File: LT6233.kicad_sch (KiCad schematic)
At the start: 15 parts, among them U3001 LT6233CS6#TRMPBF, U3002 PBSS4230T,215

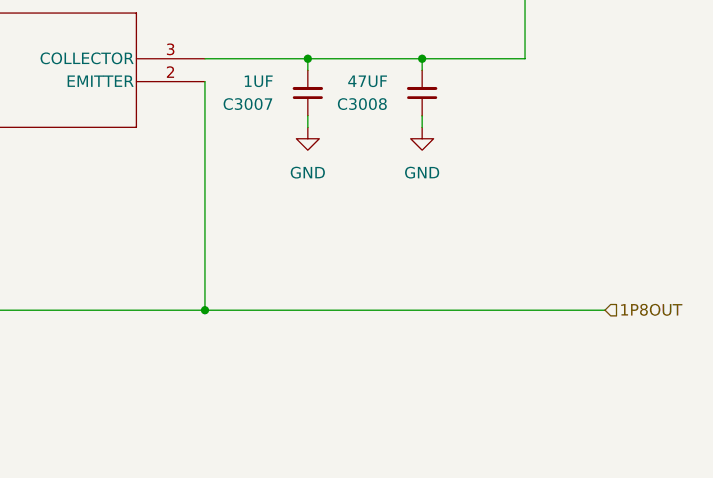
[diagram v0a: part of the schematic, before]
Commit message: resolve duplicate power flag
kicad 8 complains about two power flags on VSS1P8V net,
one each on ADC0 and ADC1 pages.  Consolidate to one
flag on the U35_LT6233 page.
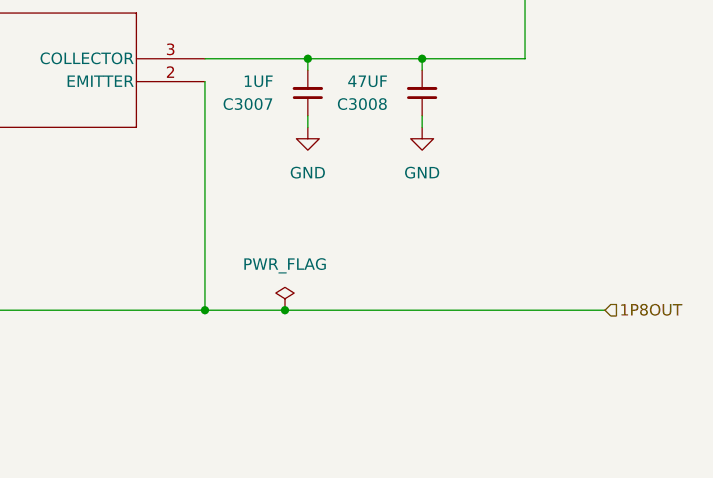
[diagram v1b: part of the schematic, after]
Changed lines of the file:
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@@
+	)
+	(junction
+		(at 217.17 113.03)
+		(diameter 0)
+		(color 0 0 0 0)
 	)
 	(junction
@@
 	(wire
 		(pts
+			(xy 217.17 113.03) (xy 252.73 113.03)
+		)
+		(stroke
+			(width 0)
+			(type default)
+		)
+	)
+	(wire
+		(pts
 			(xy 232.41 86.36) (xy 232.41 85.09)
 		)
@@
 	(wire
 		(pts
-			(xy 208.28 113.03) (xy 252.73 113.03)
+			(xy 208.28 113.03) (xy 217.17 113.03)
 		)
 		(stroke
@@
 					(unit 1)
 				)
+			)
+		)
+	)
+	(symbol
+		(lib_id "power:PWR_FLAG")
+		(at 217.17 113.03 0)
+		(unit 1)
+		(exclude_from_sim no)
+		(in_bom yes)
+		(on_board yes)
+		(dnp no)
+		(fields_autoplaced yes)
+		(property "Reference" "#FLG04"
+			(at 217.17 111.125 0)
+			(effects
+				(font
+					(size 1.27 1.27)
+				)
+				(hide yes)
+			)
+		)
+		(property "Value" "PWR_FLAG"
+			(at 217.17 107.95 0)
+			(effects
+				(font
+					(size 1.27 1.27)
+				)
+			)
+		)
+		(property "Footprint" ""
+			(at 217.17 113.03 0)
+			(effects
+				(font
+					(size 1.27 1.27)
+				)
+				(hide yes)
+			)
+		)
+		(property "Datasheet" "~"
+			(at 217.17 113.03 0)
+			(effects
+				(font
+					(size 1.27 1.27)
+				)
+				(hide yes)
+			)
+		)
+		(property "Description" "Special symbol for telling ERC where power comes from"
+			(at 217.17 113.03 0)
+			(effects
+				(font
+					(size 1.27 1.27)
+				)
+				(hide yes)
+			)
+		)
+		(pin "1"
+		)
+		(instances
+			(project ""
+				(path "/00000000-0000-0000-0000-000000000003/00000000-0000-0000-0000-000000000002/84286640-adb6-4b0c-9fb1-cd512b643b0c"
+					(reference "#FLG04")
+					(unit 1)
+				)
